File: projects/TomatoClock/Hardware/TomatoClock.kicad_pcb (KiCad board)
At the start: 2 copper layers, 6 parts, among them J3 Screen, J4 Ultrasonic, U1 ATmega328P-PU, Y1 16MHz

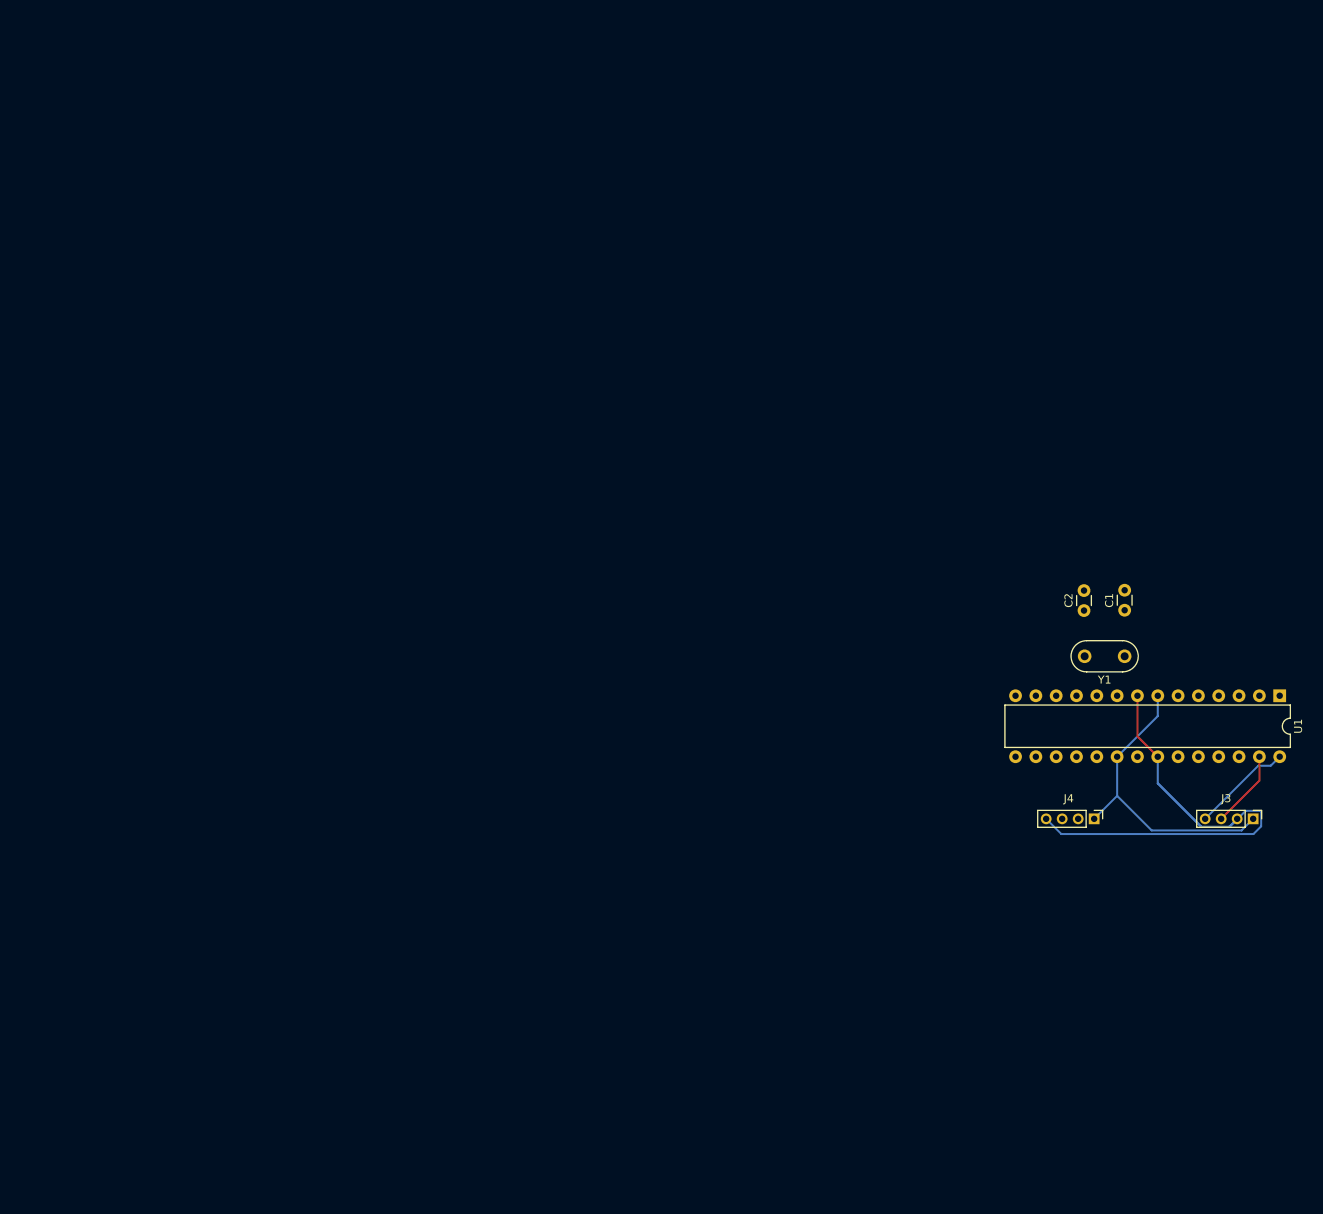
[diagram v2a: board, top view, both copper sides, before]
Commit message: TomatoClock: Change U1 from ATmega328p to STM32F103C8T6; Add power management citcuit; Update PCB
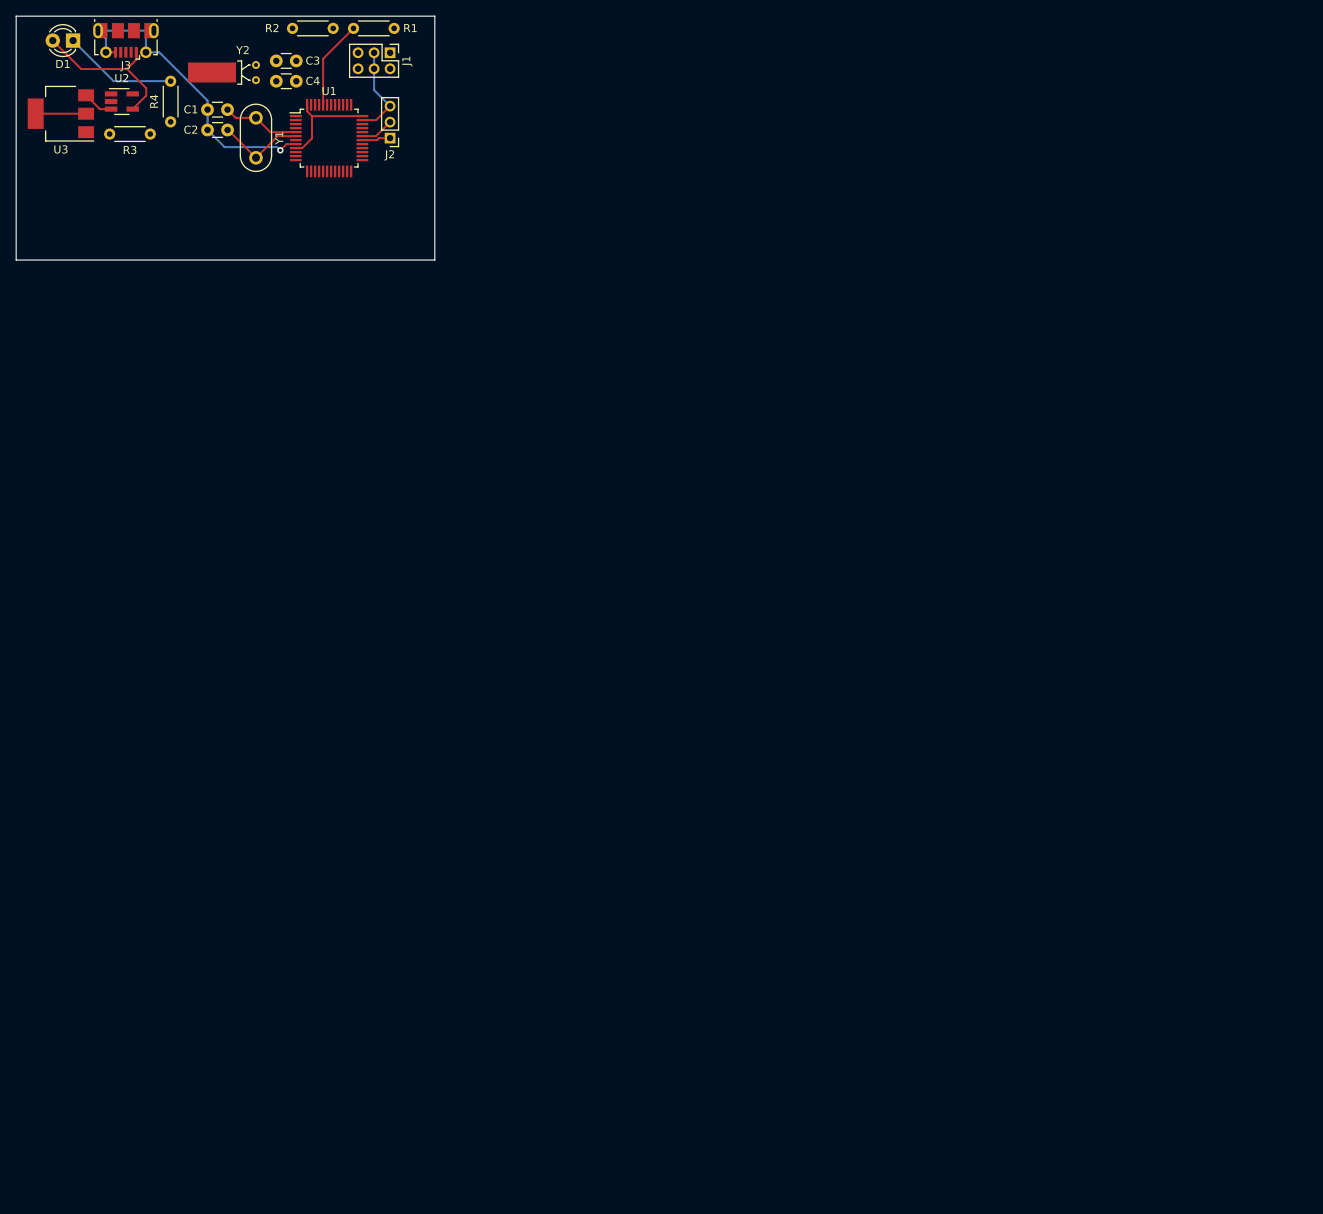
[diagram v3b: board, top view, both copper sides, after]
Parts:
- removed J4: Ultrasonic, Connector_PinHeader_2.00mm:PinHeader_1x04_P2.00mm_Vertical
- added C3: 22pF, Capacitor_THT:C_Disc_D3.0mm_W1.6mm_P2.50mm, F.Cu at (66.0, 36.1)
- added C4: 22pF, Capacitor_THT:C_Disc_D3.0mm_W1.6mm_P2.50mm, F.Cu at (66.0, 38.6)
- added D1: Charge, LED_THT:LED_D3.0mm, F.Cu at (40.6, 33.5)
- added J1: Boot, Connector_PinHeader_2.00mm:PinHeader_2x03_P2.00mm_Vertical, F.Cu at (80.3, 35.1)
- added J2: UART, Connector_PinHeader_2.00mm:PinHeader_1x03_P2.00mm_Vertical, F.Cu at (80.3, 45.7)
- added R1: 100k, Resistor_THT:R_Axial_DIN0204_L3.6mm_D1.6mm_P5.08mm_Horizontal, F.Cu at (80.8, 32.0)
- added R2: 100k, Resistor_THT:R_Axial_DIN0204_L3.6mm_D1.6mm_P5.08mm_Horizontal, F.Cu at (68.1, 32.0)
- added R3: 10k, Resistor_THT:R_Axial_DIN0204_L3.6mm_D1.6mm_P5.08mm_Horizontal, F.Cu at (45.2, 45.2)
- added R4: 10k, Resistor_THT:R_Axial_DIN0204_L3.6mm_D1.6mm_P5.08mm_Horizontal, F.Cu at (52.8, 38.6)
- added U2: WS4518E, Package_TO_SOT_SMD:SOT-23-5_HandSoldering, F.Cu at (46.7, 41.1)
- added U3: AP1117-33, Package_TO_SOT_SMD:SOT-223-3_TabPin2, F.Cu at (39.1, 42.7)
- added Y2: 32.768kHz, Crystal:Crystal_DS26_D2.0mm_L6.0mm_Horizontal_1EP_style1, F.Cu at (63.5, 36.6)
- J3: value Screen -> USB_B_Micro; footprint Connector_PinHeader_2.00mm:PinHeader_1x04_P2.00mm_Vertical -> Connector_USB:USB_Micro-B_Molex-105017-0001
- U1: value ATmega328P-PU -> STM32F103C8T6; footprint Package_DIP:DIP-28_W7.62mm -> Package_QFP:LQFP-48_7x7mm_P0.5mm
- Y1: value 16MHz -> 8MHz
- moved J3 171.2 mm to (47.2, 33.5), turned to 180 degrees
- moved U1 137.8 mm to (72.6, 45.7), turned to 0 degrees
- moved Y1 127.8 mm to (63.5, 43.2), turned to 270 degrees
- moved C1 127.2 mm to (59.9, 42.2), turned to 180 degrees
- moved C2 122.8 mm to (59.9, 44.7), turned to 180 degrees
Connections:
- C1 pad 1: GND -> Net-(C1-Pad1)
- C1 pad 2: Net-(C1-Pad2) -> GND
- J3 pad 1: +3V3 -> VBUS
- J3 pad 2: GND -> (no net)
- J3 pad 3: SDA -> (no net)
- J3 pad 4: SCL -> (no net)
- U1 pad 1: (no net) -> +BATT
- U1 pad 10: Net-(C2-Pad1) -> (no net)
- U1 pad 20: +3V3 -> BOOT1
- U1 pad 22: GND -> (no net)
- U1 pad 23: (no net) -> GND
- U1 pad 24: (no net) -> +3V3
- U1 pad 27: SDA -> (no net)
- U1 pad 28: SCL -> (no net)
- U1 pad 3: (no net) -> Net-(C3-Pad1)
- U1 pad 4: (no net) -> Net-(C4-Pad1)
- U1 pad 5: (no net) -> Net-(C1-Pad1)
- U1 pad 6: (no net) -> Net-(C2-Pad1)
- U1 pad 7: +3V3 -> (no net)
- U1 pad 9: Net-(C1-Pad2) -> +3V3
- Y1 pad 1: Net-(C1-Pad2) -> Net-(C1-Pad1)
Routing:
- net VBUS: track 0.00 -> 20.0 mm
- net GND: track 71.8 -> 52.5 mm, vias 0 -> 1
- net +3V3: track 38.1 -> 19.6 mm
- net Net-(D1-Pad1): track 0.00 -> 14.3 mm
- net SCL: track 12.5 -> 0.00 mm
- net BOOT0: track 0.00 -> 11.1 mm
- net Net-(C2-Pad1): track 0.11 -> 11.1 mm
- net SDA: track 9.74 -> 0.00 mm
- net Net-(C1-Pad1): track 0.00 -> 9.70 mm
- net Net-(J2-Pad2): track 0.00 -> 4.18 mm
- net +BATT: track 0.00 -> 3.83 mm
- net Net-(J2-Pad1): track 0.00 -> 3.56 mm
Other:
- board outline added: 52.3 x 30.5 mm

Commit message: TomatoClock: Update PCB and Gerber files
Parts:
- added BZ1: Buzzer, Buzzer_Beeper:Buzzer_15x7.5RM7.6, F.Cu at (84.8, 100.1)
- added H1: hole, MountingHole:MountingHole_2.2mm_M2, F.Cu at (73.7, 81.3)
- added H2: hole, MountingHole:MountingHole_2.2mm_M2, F.Cu at (73.7, 107.2)
- added H3: hole, MountingHole:MountingHole_2.2mm_M2, F.Cu at (118.9, 81.3)
- added H4: hole, MountingHole:MountingHole_2.2mm_M2, F.Cu at (118.9, 107.2)
- added J4: Ultrasonic, Connector_PinSocket_2.00mm:PinSocket_1x04_P2.00mm_Vertical, F.Cu at (94.0, 106.2)
- added J5: Buttons, Connector_PinHeader_2.00mm:PinHeader_1x05_P2.00mm_Vertical, F.Cu at (105.9, 106.2)
- added J6: Battery, Connector_Molex:Molex_Micro-Latch_53253-0270_1x02_P2.00mm_Vertical, F.Cu at (98.6, 82.0)
- added Q1: S9014, Package_TO_SOT_THT:TO-92, F.Cu at (92.5, 98.3)
- R1, R2, R3, R4: footprint Resistor_THT:R_Axial_DIN0204_L3.6mm_D1.6mm_P5.08mm_Horizontal -> Resistor_SMD:R_0603_1608Metric
- moved R2 68.8 mm to (115.3, 82.0), turned to 90 degrees
- moved U3 68.5 mm to (89.7, 88.9), turned to 0 degrees
- moved D1 68.3 mm to (89.4, 81.3)
- moved C2 67.1 mm to (102.9, 96.3), turned to 90 degrees
- moved C1 66.5 mm to (98.6, 96.3), turned to 90 degrees
- moved Y1 66.4 mm to (98.6, 99.6), turned to 0 degrees
- moved C3 64.4 mm to (102.9, 88.9), turned to 270 degrees
- moved Y2 62.5 mm to (102.9, 85.1)
- moved C4 59.9 mm to (98.6, 88.9), turned to 270 degrees
- moved U1 59.4 mm to (110.0, 91.9)
- moved J3 59.1 mm to (81.3, 81.8)
- moved J2 59.0 mm to (118.1, 90.9)
- moved R4 57.5 mm to (91.4, 81.3)
- moved J1 55.9 mm to (108.0, 83.6), turned to 90 degrees
- moved U2 55.6 mm to (75.2, 88.9), turned to 180 degrees
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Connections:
- J1 pad 2: Net-(J1-Pad2) -> +3V3
- J1 pad 3: GND -> Net-(J1-Pad3)
- J1 pad 4: GND -> Net-(J1-Pad4)
- J1 pad 5: Net-(J1-Pad5) -> GND
- J1 pad 6: +3V3 -> GND
- R1 pad 1: Net-(J1-Pad2) -> Net-(J1-Pad3)
- R2 pad 2: Net-(J1-Pad5) -> Net-(J1-Pad4)
- U1 pad 14: (no net) -> LEFT
- U1 pad 15: (no net) -> MIDDLE
- U1 pad 16: (no net) -> RIGHT
- U1 pad 17: (no net) -> US_TRIG
- U1 pad 18: (no net) -> US_ECHO
- U1 pad 19: (no net) -> BUZZER
- Y2 pad 3: (no net) -> GND
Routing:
- net GND: track 52.5 -> 179.5 mm, vias 1 -> 8
- net +3V3: track 19.6 -> 84.1 mm, vias 0 -> 5
- net +BATT: track 3.83 -> 50.6 mm, vias 0 -> 2
- net BUZZER: track 0.00 -> 21.7 mm, vias 0 -> 1
- net US_TRIG: track 0.00 -> 20.9 mm, vias 0 -> 1
- net US_ECHO: track 0.00 -> 20.5 mm, vias 0 -> 1
- net Net-(R4-Pad2): track 0.00 -> 18.1 mm
- net BOOT1: track 0.00 -> 15.1 mm
- net Net-(D1-Pad1): track 14.3 -> 2.37 mm
- net RIGHT: track 0.00 -> 11.4 mm
- net MIDDLE: track 0.00 -> 10.8 mm
- net Net-(C4-Pad1): track 0.00 -> 10.7 mm
- net LEFT: track 0.00 -> 10.1 mm
- net Net-(C3-Pad1): track 0.00 -> 7.97 mm
- net Net-(BZ1-Pad1): track 0.00 -> 7.94 mm
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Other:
- board size 52.3 x 30.5 mm -> 50.3 x 31 mm
- board text added: "0"
- board text added: "1"
- board text added: "BOOT0"
- board text added: "BOOT1"
- board text added: "Buttons"
- board text added: "By yangshunhuai"
- board text added: "REV 1.0"
- board text added: "TomatoClock"
- board text added: "UART"
- board text added: "Ultrasonic"

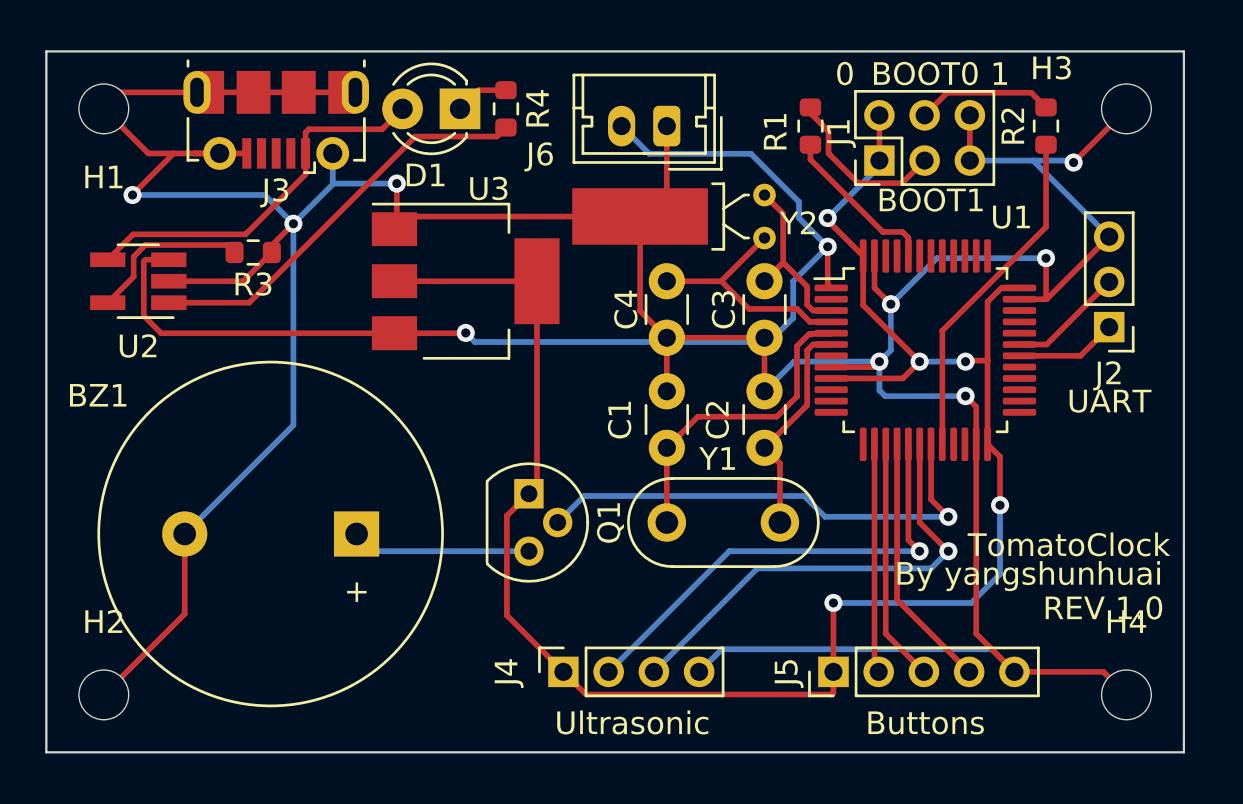
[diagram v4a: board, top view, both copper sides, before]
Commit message: TomatoClock: Update C1-C4 from TH to SMD
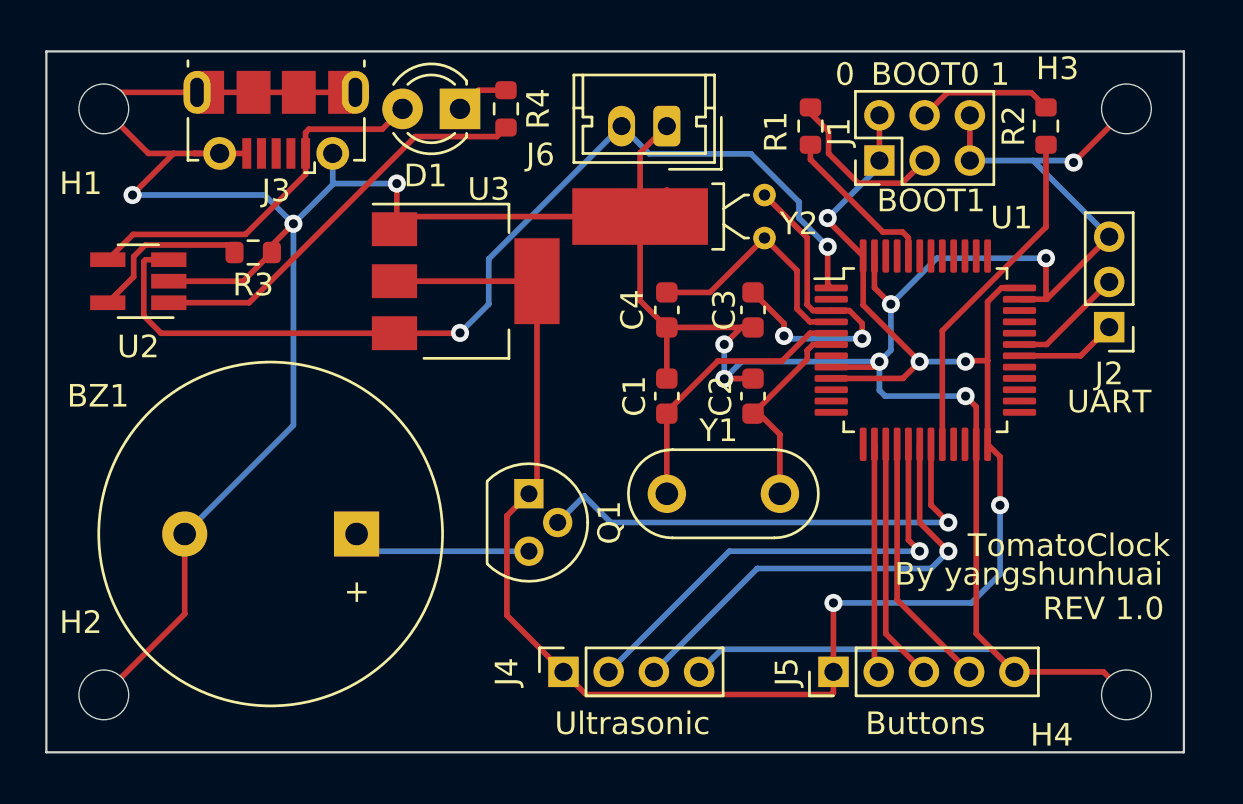
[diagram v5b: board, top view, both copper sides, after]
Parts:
- C1, C2, C3, C4: footprint Capacitor_THT:C_Disc_D3.0mm_W1.6mm_P2.50mm -> Capacitor_SMD:C_0603_1608Metric
- moved C2 2.34 mm to (102.4, 94.0)
- moved C1 2.29 mm to (98.6, 94.0)
- moved C3 1.37 mm to (102.4, 90.2)
- moved C4 1.27 mm to (98.6, 90.2)
- moved Y1 1.27 mm to (98.6, 98.3)
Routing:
- net Net-(C3-Pad1): track 7.97 -> 15.1 mm, vias 0 -> 2
- net +BATT: track 50.6 -> 43.6 mm
- net GND: track 179.5 -> 183.7 mm, vias 8 -> 10
- net Net-(C1-Pad1): track 14.0 -> 12.3 mm
- net Net-(C2-Pad1): track 9.84 -> 9.15 mm
